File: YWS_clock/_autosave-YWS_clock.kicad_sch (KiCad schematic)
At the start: 32 parts, among them U2 ATmega328-PU, Y1 Crystal_16MHz

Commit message: Update Buzzer and joystick
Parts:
- added BT1: Battery_Cell, footprints:BatteryHolder_Keystone_106_1x20mm, symbol HPS:Battery_Cell
- added BZ?: Buzzer, footprints:Buzzer_TDK_PS1240P02BT_D12.2mm_H6.5mm, symbol HPS:Buzzer
- added C5: C_0805_0.1uf, footprints:C_0805_2012Metric, symbol HPS:C_0805_0.1uf
- added C6, C7: C_0805_1uf, footprints:C_0805_2012Metric, symbol HPS:C_0805_1uf
- added D1: LED_0805, footprints:LED_0805_2012Metric, symbol HPS:LED_0805
- added J1: Conn_01x06, footprints:PinHeader_1x06_P2.54mm_Vertical, symbol HPS:Conn_01x06
- added J2: PJ-102AH, footprints:PJ-102AH, symbol HPS:PJ-102AH
- added J?: Conn_01x05, footprints:PinHeader_1x05_P2.54mm_Vertical, symbol HPS:Conn_01x05
- added R2, R5, R6: R_0805_2.2K, footprints:R_0805_2012Metric, symbol HPS:R_0805_2.2K
- added R3, R4: R_0805_47, footprints:R_0805_2012Metric, symbol HPS:R_0805_47
- added SW1: Omron_B3F_SPST, footprints:SW_SPST_Omron_B3FS-100xP, symbol HPS:Omron_B3F_SPST
- added U1: L7805, footprints:TO-220-3_Horizontal_TabDown, symbol HPS:L7805
- added Y2: Crystal_16MHz, footprints:Crystal_SMD_HC49-SD, symbol HPS:Crystal_16MHz
- gave numbers to parts that had none: 21
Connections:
- net VCC is gone; now on net GND: C10.1, C11.1, C12.1, C13.1, C14.1, C15.1, C2.1, C8.1, C9.1, R1.1, R10.1, R7.1, R8.1, R9.1, U2.20 (AVCC), U2.7 (VCC), U4.19 (V+), U5.19 (V+), U6.19 (V+), U7.19 (V+)
- net GND: now also U3.4 (GND), U3.8 (VCC), BT1.2 (-), C6.2, C7.1, C7.2, D1.1 (K), J1.1 (Pin_1), J1.2 (Pin_2), J2.2 (OUT), J?.1 (Pin_1), J?.2 (Pin_2), R5.1, R6.1, SW1.1 (A), SW1.2 (A), U1.2 (GND), U1.3 (OUT)
- net LED_SCK: now also U2.15 (PB1), U2.18 (PB4), R2.1; no longer U2.17 (PB3), U2.19 (PB5)
- net RESET: now also C5.1, SW1.3 (B), SW1.4 (B)
- net RXD: now also U2.12 (PD6), R3.2; no longer U2.2 (PD0)
- net TXD: now also U2.13 (PD7), R4.1; no longer U2.4 (PD2)
- net at U5.12 (LOAD): now also U2.16 (PB2), U4.12 (LOAD), U6.12 (LOAD), U7.12 (LOAD)
- net at U5.13 (CLK): now also U2.19 (PB5), U4.13 (CLK), U6.13 (CLK), U7.13 (CLK)
- net at U3.1 (X1): now also Y2.1
- net at U3.2 (X2): now also Y2.2
- net at U3.3 (VBAT): now also BT1.1 (+)
- net at U3.5 (SDA): now also U2.3 (PD1), R5.2
- net at U3.6 (SCL): now also U2.2 (PD0), R6.2
- net at U4.1 (DIN): now also U2.17 (PB3)
- net SW: now reaches U2.11 (PD5)
- net SW: now also J?.5 (Pin_5)
- net VRx: now reaches U2.23 (PC0)
- net VRx: now also J?.3 (Pin_3)
- net VRy: now reaches U2.24 (PC1)
- net VRy: now also J?.4 (Pin_4)
- new net: C6.1, J2.1 (POLE), U1.1 (IN)
- new net: C5.2, J1.6 (Pin_6)
- new net: J1.5 (Pin_5), R3.1
- new net: J1.4 (Pin_4), R4.2
- new net: D1.2 (A), R2.2
- no-connect marks 0 -> 3
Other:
- note added: "DS1307"
- note added: "LED"
- note added: "Power Input"
- note added: "Serial"
- note added: "Vf = 2v Vr = 3v 10mcd @ 1.35mA therefore R = 2.2K0hm"
- moved on the sheet: C1, C10, C11, C12, C13, C14, C15, C2, C3, C4, C8, C9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

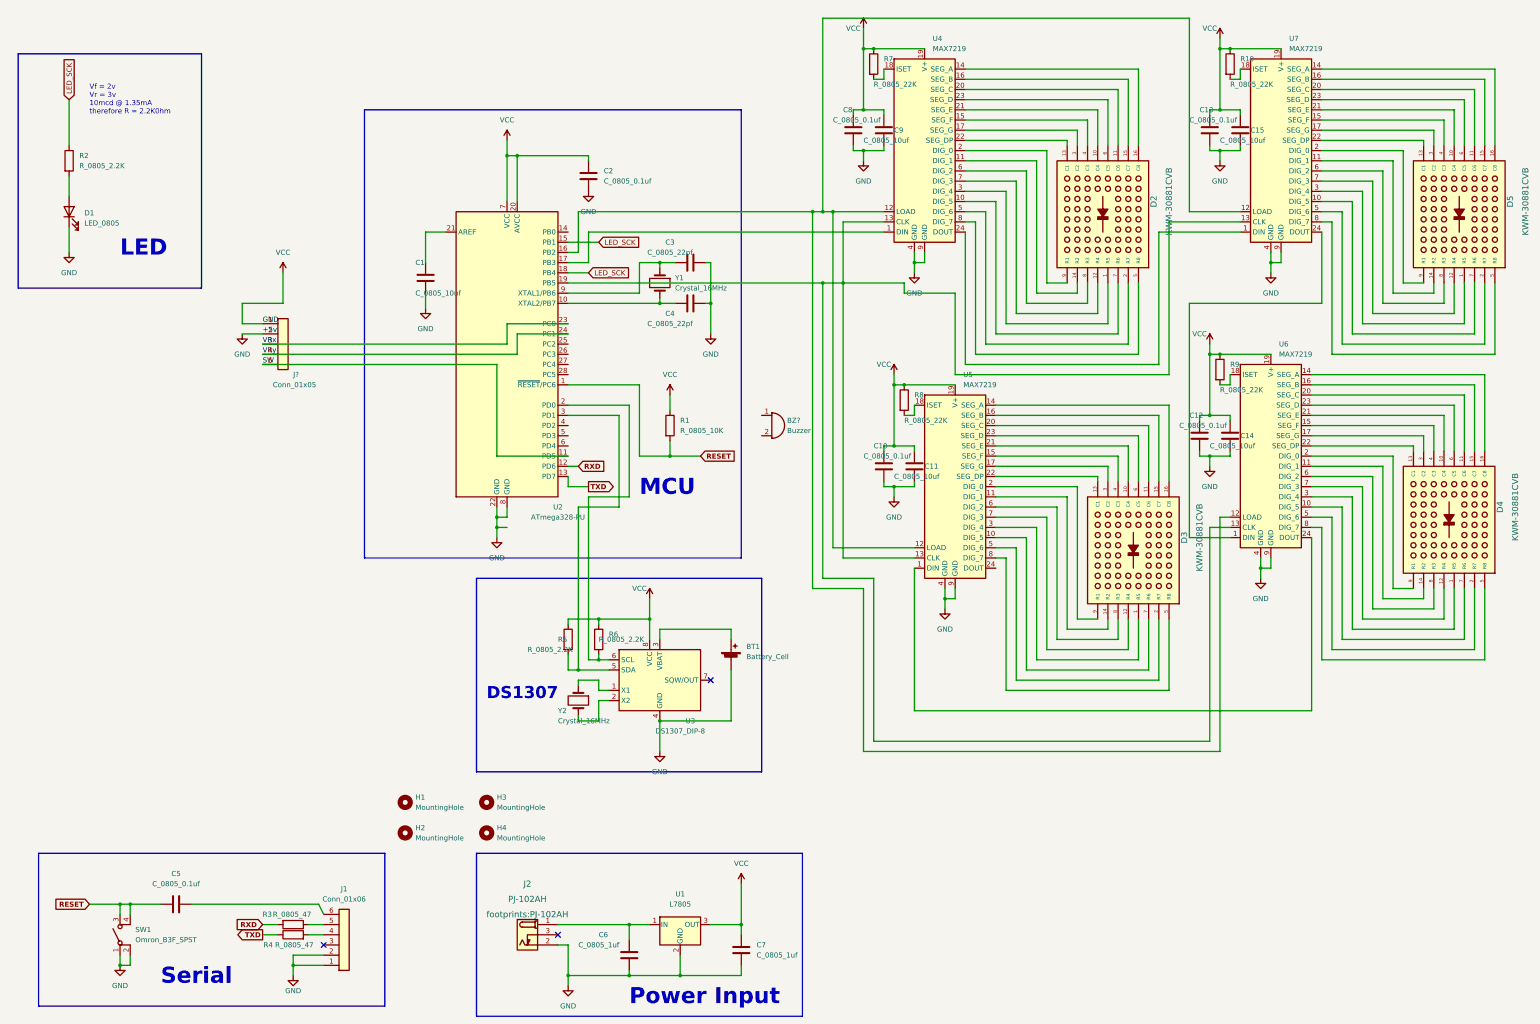
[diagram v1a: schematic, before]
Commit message: update PCB and Schematic with dot matrix
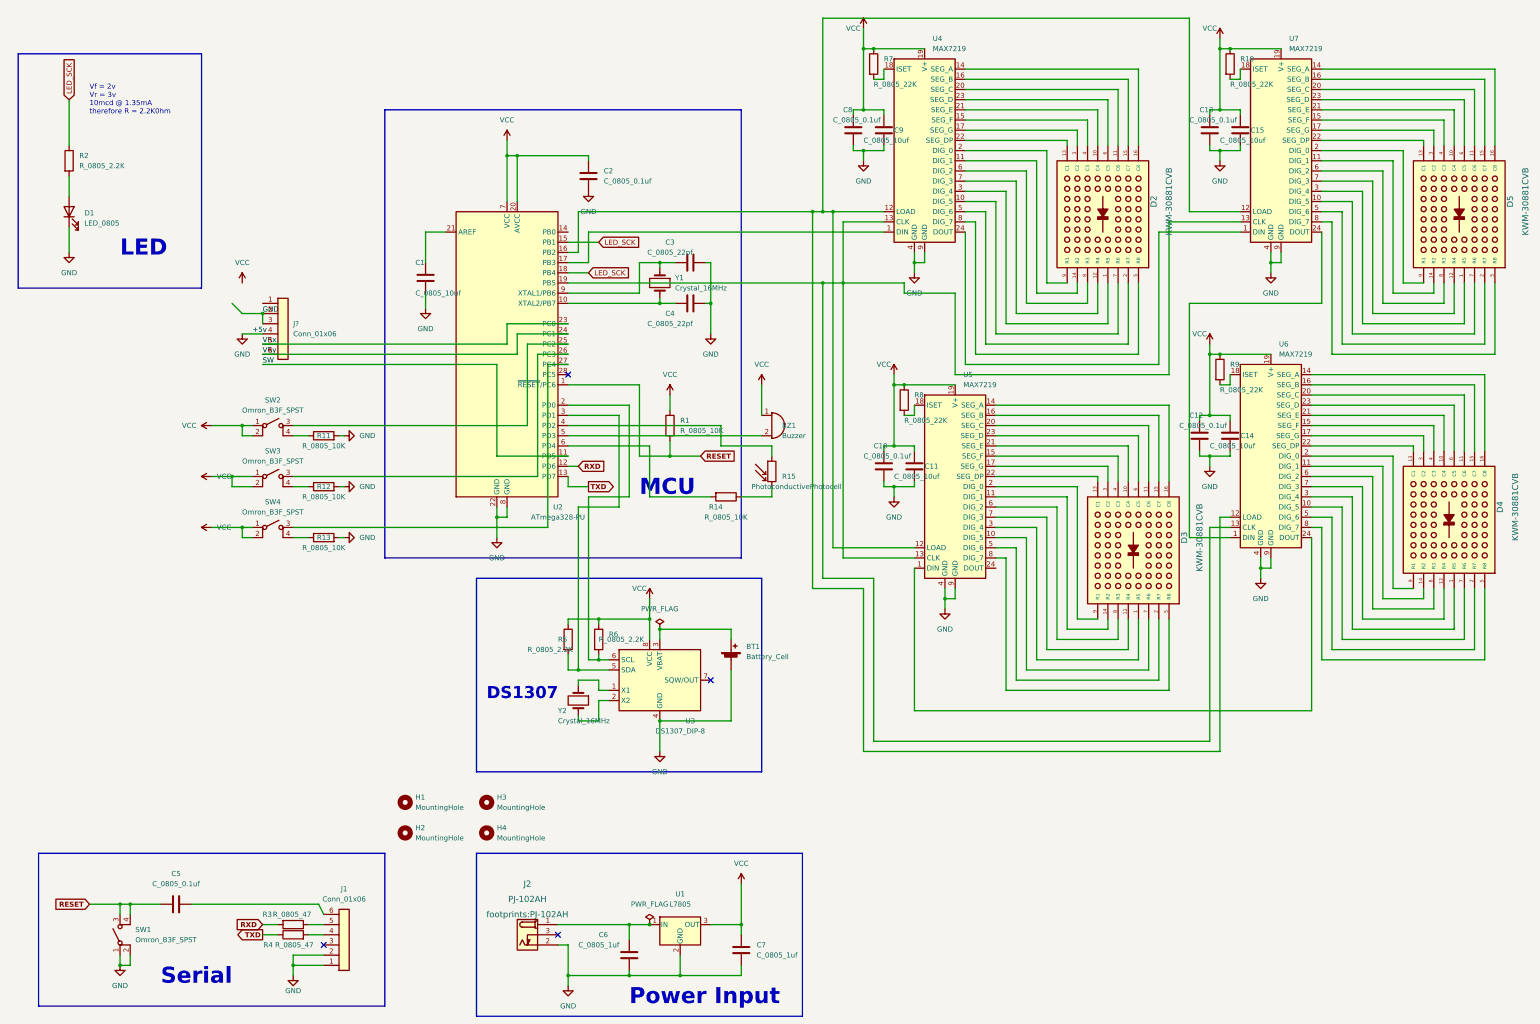
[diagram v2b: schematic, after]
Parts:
- removed J?: Conn_01x05, footprints:PinHeader_1x05_P2.54mm_Vertical, symbol HPS:Conn_01x05
- added J?: Conn_01x06, footprints:PinHeader_1x06_P2.54mm_Vertical, symbol HPS:Conn_01x06
- added R11, R12, R13, R14: R_0805_10K, footprints:R_0805_2012Metric, symbol HPS:R_0805_10K
- added R15: PhotoconductivePhotocell, footprints:R_LDR_4.9x4.2mm_P2.54mm_Vertical, symbol HPS:PhotoconductivePhotocell
- added SW2, SW3, SW4: Omron_B3F_SPST, footprints:SW_SPST_Omron_B3FS-100xP, symbol HPS:Omron_B3F_SPST
- gave numbers to parts that had none: 1
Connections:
- net GND: now also J?.2 (Pin_2), J?.3 (Pin_3), J?.4 (Pin_4), R11.2, R12.2, R13.2; no longer C10.1, C11.1, C12.1, C13.1, C14.1, C15.1, C2.1, C7.1, C8.1, C9.1, R1.1, R10.1, R5.1, R6.1, R7.1, R8.1, R9.1, U1.3 (OUT), U2.20 (AVCC), U2.7 (VCC), U3.8 (VCC), U4.19 (V+), U5.19 (V+), U6.19 (V+), U7.19 (V+)
- net VRx: now also J?.5 (Pin_5)
- net VRy: now also J?.6 (Pin_6)
- net at U2.25 (PC2): now also SW2.3 (B)
- net at U2.26 (PC3): now also SW3.3 (B)
- net at U2.27 (PC4): now also SW4.3 (B)
- net at U2.4 (PD2): now also R15.1
- net at U2.5 (PD3): now also BZ1.2 (+)
- net at U2.6 (PD4): now also R14.2
- net VCC: now reaches BZ1.1 (-)
- net VCC: now also C10.1, C11.1, C12.1, C13.1, C14.1, C15.1, C2.1, C7.1, C8.1, C9.1, R1.1, R10.1, R5.1, R6.1, R7.1, R8.1, R9.1, U1.3 (OUT), U2.20 (AVCC), U2.7 (VCC), U3.8 (VCC), U4.19 (V+), U5.19 (V+), U6.19 (V+), U7.19 (V+), SW2.1 (A), SW2.2 (A), SW3.1 (A), SW3.2 (A), SW4.1 (A), SW4.2 (A)
- new net: R14.1, R15.2
- new net: R13.1, SW4.4 (B)
- new net: R11.1, SW2.4 (B)
- new net: R12.1, SW3.4 (B)
- no-connect marks 3 -> 4
